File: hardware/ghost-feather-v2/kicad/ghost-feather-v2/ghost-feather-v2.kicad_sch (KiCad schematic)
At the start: 72 parts, among them J1 STM32F722RETx, J2 nRF52810, J3 Conn_01x03, J4 Conn_01x03, J5 Conn_01x03, J6 Conn_01x03, Q1 BSS138, Q2 BSS138, Q3 BSS138, Q4 BSS138, SW1 BOOT0, U1 STM32F722RETx, U2 BMI088, U2 nRF52810-QCxx, U3 IIS2MDCTR, U4 BMP390, X3 32MHz, X4 32.768kHz

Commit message: feat: hadware: wip: Add UBSC
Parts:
- added J7: USB_C_Receptacle_USB2.0, symbol Connector:USB_C_Receptacle_USB2.0
- added R19, R20: 5k1, symbol Device:R_Small
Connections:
- net GND: now also J7.A1 (GND), J7.A12 (GND), J7.B1 (GND), J7.B12 (GND), J7.S1 (SHIELD), R19.2, R20.2
- new net: J7.A4 (VBUS), J7.A9 (VBUS), J7.B4 (VBUS), J7.B9 (VBUS)
- new net: J7.A5 (CC1), R20.1
- new net: J7.A6 (D+), J7.B6 (D+)
- new net: J7.A7 (D-), J7.B7 (D-)
- new net: J7.B5 (CC2), R19.1
- no-connect marks 9 -> 11

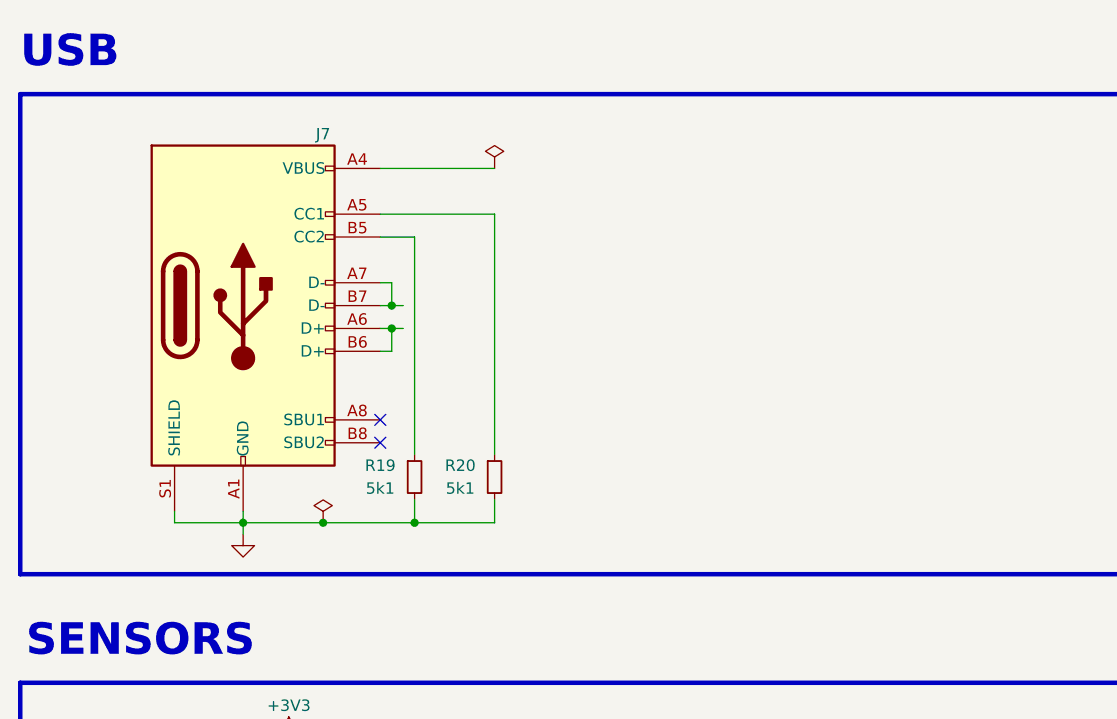
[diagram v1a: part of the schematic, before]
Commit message: feat: hadware: Finish USBC and add TVS diode protection
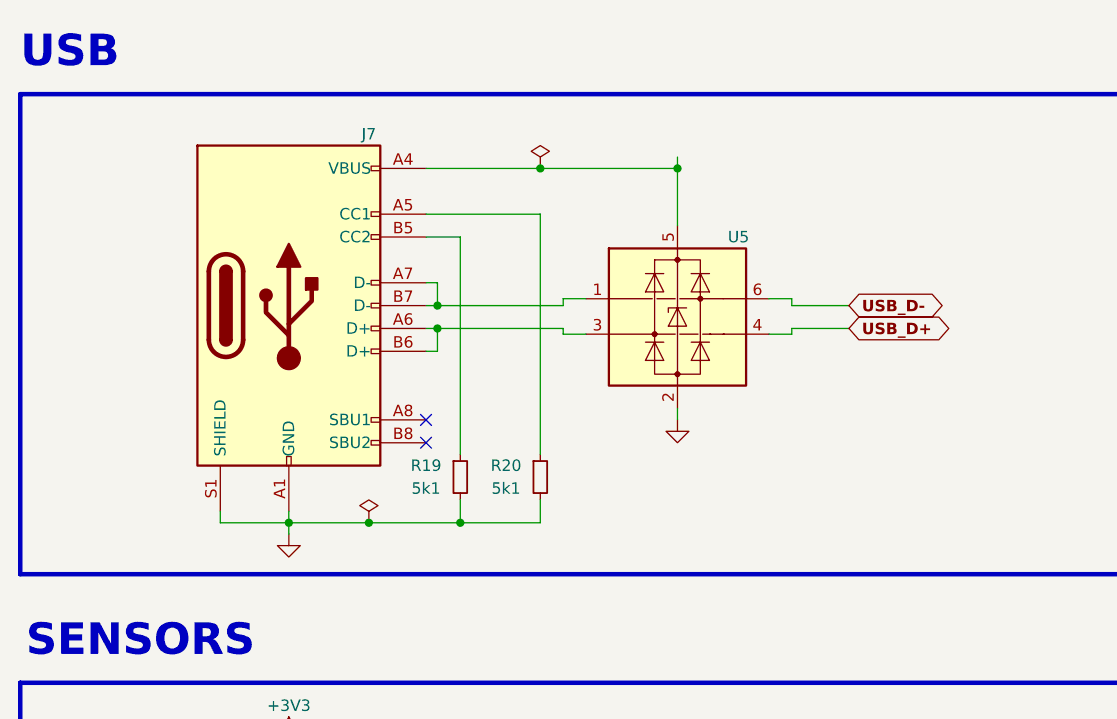
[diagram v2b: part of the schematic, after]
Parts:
- added U5: USBLC6-2SC6_MOD, Package_TO_SOT_SMD:SOT-23-6, symbol Power_Protection:USBLC6-2SC6_MOD
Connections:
- net GND: now also U5.2 (GND)
- net USB_D+: now also U5.4 (I/O4)
- net USB_D-: now also U5.6 (I/O6)
- net at J7.A4 (VBUS), J7.A9 (VBUS), J7.B4 (VBUS)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: now also U5.5 (VBUS)
- net at J7.A6 (D+), J7.B6 (D+): now also U5.3 (I/O3)
- net at J7.A7 (D-), J7.B7 (D-): now also U5.1 (I/O1)
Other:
- moved on the sheet: J7, R19, R20

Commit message: feat: hadware: Add STM32F7 LSE
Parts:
- added C35, C36: 12p, symbol Device:C_Small
- added X2: 32.768kHz, symbol Device:Crystal_Small
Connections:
- net GND: now also C35.2, C36.2
- net USART3_TX: now reaches U2.10 (P0.12)
- net USART3_TX: now also U1.51 (PC10)
- net USART3_RX: now reaches U2.11 (P0.14)
- net USART3_RX: now also U1.52 (PC11)
- net at U1.3 (PC14): now also C36.1, X2.2
- net USART6_TX: now reaches U1.37 (PC6)
- net USART6_RX: now reaches U1.38 (PC7)
- net at U1.4 (PC15): now also C35.1, X2.1
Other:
- moved on the sheet: R1, R4, R5

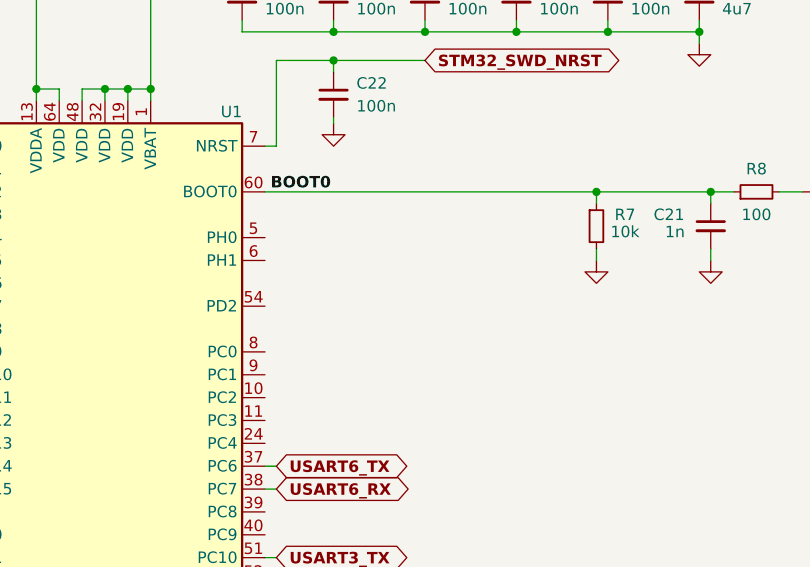
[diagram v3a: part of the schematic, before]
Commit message: feat: hadware: Add STM32F7 HSE
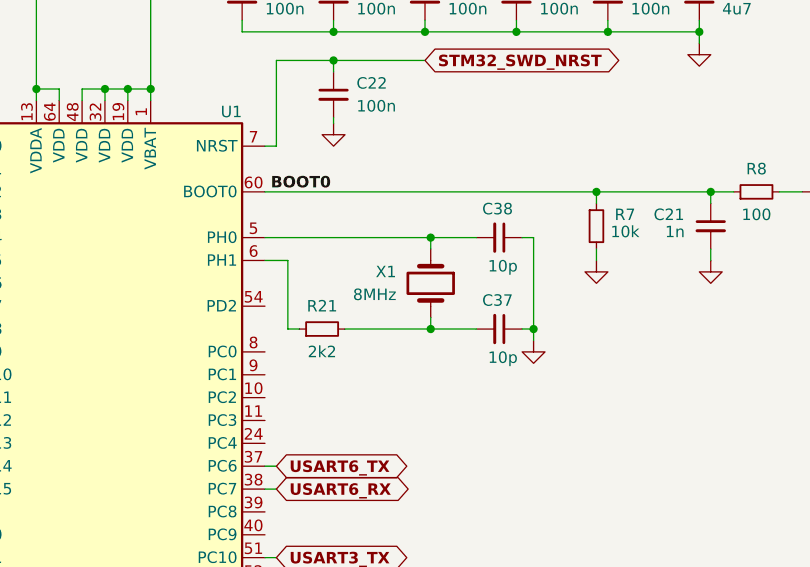
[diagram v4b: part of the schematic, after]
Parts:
- added C37, C38: 10p, symbol Device:C_Small
- added R21: 2k2, symbol Device:R_Small
- added X1: 8MHz, symbol Device:Crystal
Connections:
- net GND: now also C37.1, C38.1
- net at U1.5 (PH0): now also C38.2, X1.1
- net at U1.6 (PH1): now also R21.1
- new net: C37.2, R21.2, X1.2
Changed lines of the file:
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@@
   (junction (at 367.03 184.15) (diameter 0) (color 0 0 0 0)
   )
+  (junction (at 118.11 191.135) (diameter 0) (color 0 0 0 0)
+  )
+  (junction (at 118.11 201.295) (diameter 0) (color 0 0 0 0)
+  )
   (junction (at 341.63 194.31) (diameter 0) (color 0 0 0 0)
   )
@@
   (junction (at 273.05 116.84) (diameter 0) (color 0 0 0 0)
   )
+  (junction (at 129.54 201.295) (diameter 0) (color 0 0 0 0)
+  )
   (junction (at 196.85 124.46) (diameter 0) (color 0 0 0 0)
   )
@@
     (stroke (width 0) (type default))
   )
+  (wire (pts (xy 99.695 191.135) (xy 118.11 191.135))
+    (stroke (width 0) (type default))
+  )
   (wire (pts (xy 88.9 57.15) (xy 88.9 58.42))
     (stroke (width 0) (type default))
@@
     (stroke (width 0) (type default))
   )
+  (wire (pts (xy 128.27 191.135) (xy 129.54 191.135))
+    (stroke (width 0) (type default))
+  )
   (wire (pts (xy 76.2 48.26) (xy 76.2 48.895))
     (stroke (width 0) (type default))
@@
     (stroke (width 0) (type default))
   )
+  (wire (pts (xy 118.11 192.405) (xy 118.11 191.135))
+    (stroke (width 0) (type default))
+  )
   (wire (pts (xy 151.765 186.055) (xy 149.225 186.055))
     (stroke (width 0) (type default))
@@
     (stroke (width 0) (type default))
   )
+  (wire (pts (xy 123.19 191.135) (xy 118.11 191.135))
+    (stroke (width 0) (type default))
+  )
   (wire (pts (xy 207.645 228.6) (xy 212.09 228.6))
     (stroke (width 0) (type default))
@@
     (stroke (width 0) (type default))
   )
+  (wire (pts (xy 102.235 201.295) (xy 102.235 193.675))
+    (stroke (width 0) (type default))
+  )
   (wire (pts (xy 367.03 223.52) (xy 367.03 224.79))
     (stroke (width 0) (type default))
@@
     (stroke (width 0) (type default))
   )
+  (wire (pts (xy 123.19 201.295) (xy 118.11 201.295))
+    (stroke (width 0) (type default))
+  )
   (wire (pts (xy 62.865 216.535) (xy 64.135 216.535))
     (stroke (width 0) (type default))
@@
     (stroke (width 0) (type default))
   )
+  (wire (pts (xy 129.54 201.295) (xy 129.54 202.565))
+    (stroke (width 0) (type default))
+  )
   (wire (pts (xy 60.96 45.72) (xy 62.23 45.72))
     (stroke (width 0) (type default))
@@
     (stroke (width 0) (type default))
   )
+  (wire (pts (xy 129.54 201.295) (xy 129.54 191.135))
+    (stroke (width 0) (type default))
+  )
   (wire (pts (xy 62.865 249.555) (xy 64.135 249.555))
     (stroke (width 0) (type default))
@@
     (stroke (width 0) (type default))
   )
+  (wire (pts (xy 102.235 193.675) (xy 99.695 193.675))
+    (stroke (width 0) (type default))
+  )
   (wire (pts (xy 361.315 49.53) (xy 363.855 49.53))
     (stroke (width 0) (type default))
@@
     (stroke (width 0) (type default))
   )
+  (wire (pts (xy 128.27 201.295) (xy 129.54 201.295))
+    (stroke (width 0) (type default))
+  )
   (wire (pts (xy 79.375 271.145) (xy 81.915 271.145))
     (stroke (width 0) (type default))
@@
     (stroke (width 0) (type default))
   )
+  (wire (pts (xy 108.585 201.295) (xy 118.11 201.295))
+    (stroke (width 0) (type default))
+  )
   (wire (pts (xy 101.6 44.958) (xy 101.6 45.72))
     (stroke (width 0) (type default))
@@
     (stroke (width 0) (type default))
   )
+  (wire (pts (xy 118.11 201.295) (xy 118.11 200.025))
+    (stroke (width 0) (type default))
+  )
   (wire (pts (xy 240.03 114.3) (xy 240.03 95.25))
     (stroke (width 0) (type default))
@@
     (stroke (width 0) (type default))
   )
+  (wire (pts (xy 102.235 201.295) (xy 103.505 201.295))
+    (stroke (width 0) (type default))
+  )
   (wire (pts (xy 100.965 239.395) (xy 100.965 243.205))
     (stroke (width 0) (type default))
@@
     )
   )
+  (symbol (lib_id "Device:Crystal") (at 118.11 196.215 270) (unit 1)
+    (in_bom yes) (on_board yes) (dnp no)
+    (property "Reference" "X1" (at 114.3 194.945 90)
+      (effects (font (size 1.27 1.27)) (justify right))
+    )
+    (property "Value" "8MHz" (at 114.3 197.485 90)
+      (effects (font (size 1.27 1.27)) (justify right))
+    )
+    (property "Footprint" "" (at 118.11 196.215 0)
+      (effects (font (size 1.27 1.27)) hide)
+    )
+    (property "Datasheet" "https://www.mouser.pl/datasheet/3/184/1/ABM8AAIG.pdf" (at 118.11 196.215 0)
+      (effects (font (size 1.27 1.27)) hide)
+    )
+    (pin "1")
+    (pin "2")
+    (instances
+      (project "ghost-feather-v2"
+        (path "/f9a6fb30-e54e-4dec-8b48-0e9b06cf9ccb"
+          (reference "X1") (unit 1)
+        )
+      )
+    )
+  )
   (symbol (lib_id "power:GND") (at 285.75 236.22 0) (unit 1)
     (in_bom yes) (on_board yes) (dnp no)
@@
     )
   )
+  (symbol (lib_id "Device:C_Small") (at 125.73 191.135 270) (unit 1)
+    (in_bom yes) (on_board yes) (dnp no)
+    (property "Reference" "C38" (at 123.825 187.96 90)
+      (effects (font (size 1.27 1.27)) (justify left))
+    )
+    (property "Value" "10p" (at 124.46 194.31 90)
+      (effects (font (size 1.27 1.27)) (justify left))
+    )
+    (property "Footprint" "" (at 125.73 191.135 0)
+      (effects (font (size 1.27 1.27)) hide)
+    )
+    (property "Datasheet" "~" (at 125.73 191.135 0)
+      (effects (font (size 1.27 1.27)) hide)
+    )
+    (pin "1")
+    (pin "2")
+    (instances
+      (project "ghost-feather-v2"
+        (path "/f9a6fb30-e54e-4dec-8b48-0e9b06cf9ccb"
+          (reference "C38") (unit 1)
+        )
+      )
+    )
+  )
   (symbol (lib_id "Power_Protection:USBLC6-2SC6_MOD") (at 88.9 46.99 0) (unit 1)
     (in_bom yes) (on_board yes) (dnp no)
@@
     )
   )
+  (symbol (lib_id "Device:R_Small") (at 106.045 201.295 90) (unit 1)
+    (in_bom yes) (on_board yes) (dnp no)
+    (property "Reference" "R21" (at 106.045 198.755 90)
+      (effects (font (size 1.27 1.27)))
+    )
+    (property "Value" "2k2" (at 106.045 203.835 90)
+      (effects (font (size 1.27 1.27)))
+    )
+    (property "Footprint" "" (at 106.045 201.295 0)
+      (effects (font (size 1.27 1.27)) hide)
+    )
+    (property "Datasheet" "~" (at 106.045 201.295 0)
+      (effects (font (size 1.27 1.27)) hide)
+    )
+    (pin "1")
+    (pin "2")
+    (instances
+      (project "ghost-feather-v2"
+        (path "/f9a6fb30-e54e-4dec-8b48-0e9b06cf9ccb"
+          (reference "R21") (unit 1)
+        )
+      )
+    )
+  )
   (symbol (lib_id "Connector:Conn_ARM_SWD_TagConnect_TC2030-NL") (at 365.76 114.3 0) (unit 1)
     (in_bom no) (on_board yes) (dnp no)
@@
     )
   )
+  (symbol (lib_id "power:GND") (at 129.54 202.565 0) (unit 1)
+    (in_bom yes) (on_board yes) (dnp no)
+    (property "Reference" "#PWR056" (at 129.54 208.915 0)
+      (effects (font (size 1.27 1.27)) hide)
+    )
+    (property "Value" "GND" (at 129.54 206.375 0)
+      (effects (font (size 1.27 1.27)) hide)
+    )
+    (property "Footprint" "" (at 129.54 202.565 0)
+      (effects (font (size 1.27 1.27)) hide)
+    )
+    (property "Datasheet" "" (at 129.54 202.565 0)
+      (effects (font (size 1.27 1.27)) hide)
+    )
+    (pin "1")
+    (instances
+      (project "ghost-feather-v2"
+        (path "/f9a6fb30-e54e-4dec-8b48-0e9b06cf9ccb"
+          (reference "#PWR056") (unit 1)
+        )
+      )
+    )
+  )
   (symbol (lib_id "Device:C_Small") (at 64.135 164.465 0) (unit 1)
     (in_bom yes) (on_board yes) (dnp no) (fields_autoplaced)
@@
         )
       )
+    )
+  )
+  (symbol (lib_id "Device:C_Small") (at 125.73 201.295 270) (unit 1)
+    (in_bom yes) (on_board yes) (dnp no)
+    (property "Reference" "C37" (at 123.825 198.12 90)
+      (effects (font (size 1.27 1.27)) (justify left))
+    )
+    (property "Value" "10p" (at 124.46 204.47 90)
+      (effects (font (size 1.27 1.27)) (justify left))
+    )
+    (property "Footprint" "" (at 125.73 201.295 0)
+      (effects (font (size 1.27 1.27)) hide)
+    )
+    (property "Datasheet" "~" (at 125.73 201.295 0)
+      (effects (font (size 1.27 1.27)) hide)
+    )
+    (pin "1")
+    (pin "2")
+    (instances
+      (project "ghost-feather-v2"
+        (path "/f9a6fb30-e54e-4dec-8b48-0e9b06cf9ccb"
+          (reference "C37") (unit 1)
+        )
+      )
